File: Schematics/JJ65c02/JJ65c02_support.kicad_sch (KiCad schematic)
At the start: 38 parts, among them J1 Mini-DIN-6, J2 Barrel_Jack, J3 VIA2 PortB, J4 Arduino Jack1, J5 Arduino Jack2, J6 AudioJack2, SW1 RESET, SW2 SW_SPST, U2 NE555, U3 74HC00, U4 MAX232B, U5 74AC138, U6 LM386, U7 LM2940T-5.0/LF08, X1 1Mhz, X2 1.8Mhz

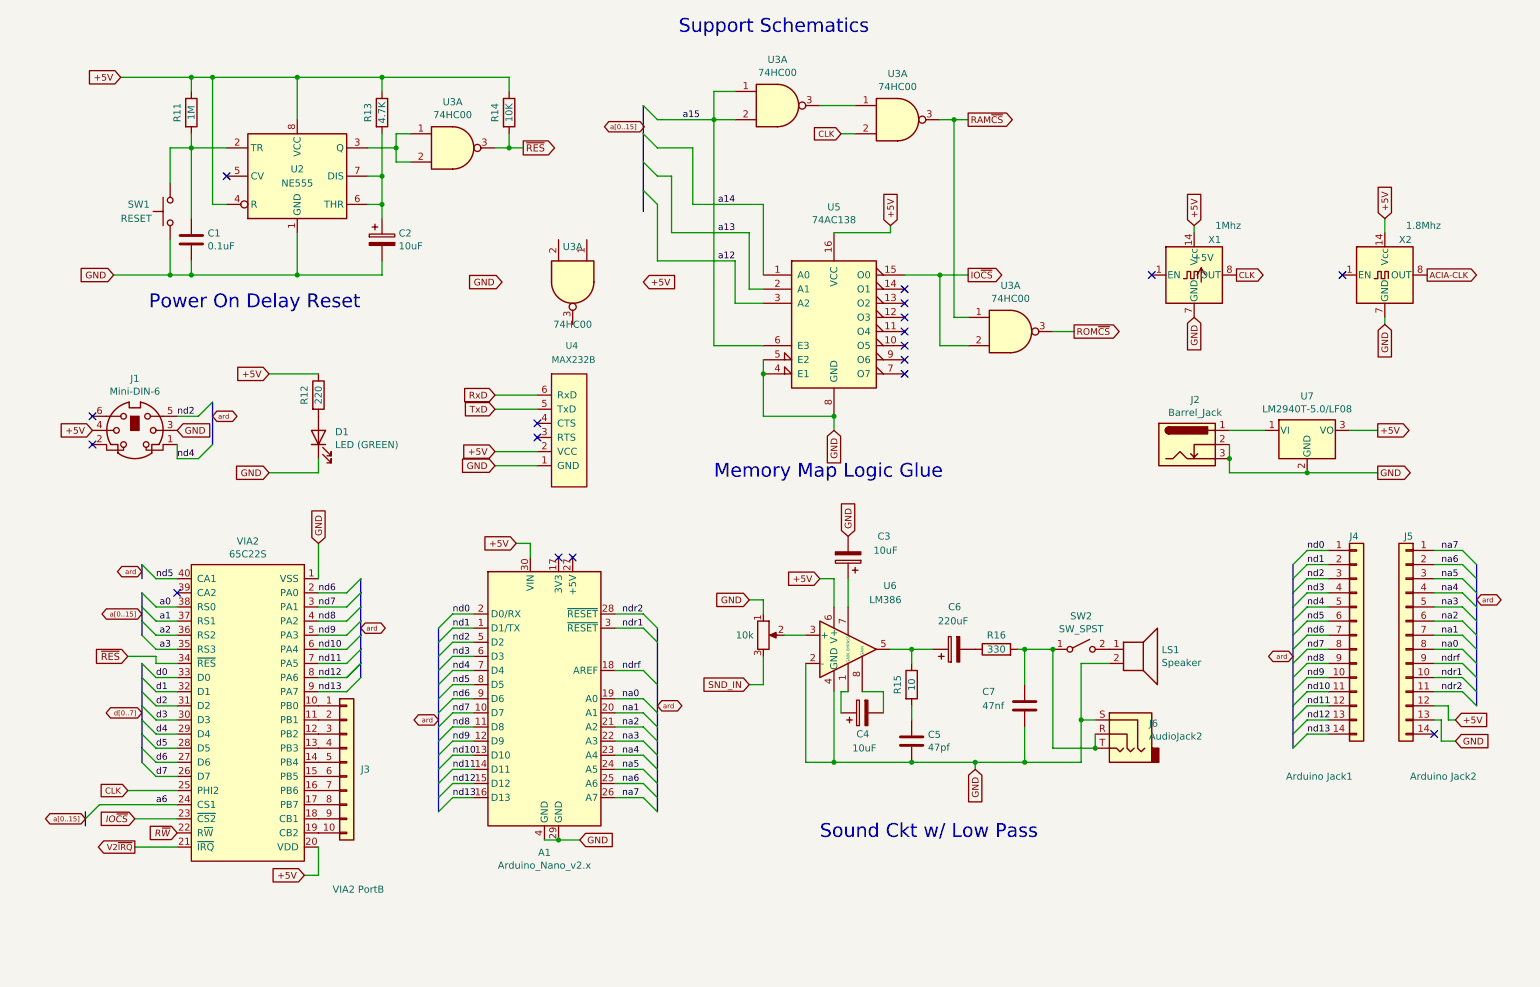
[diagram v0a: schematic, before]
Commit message: We are no longer bit-bashing sound on the VIA chip. Keep the files for future generations
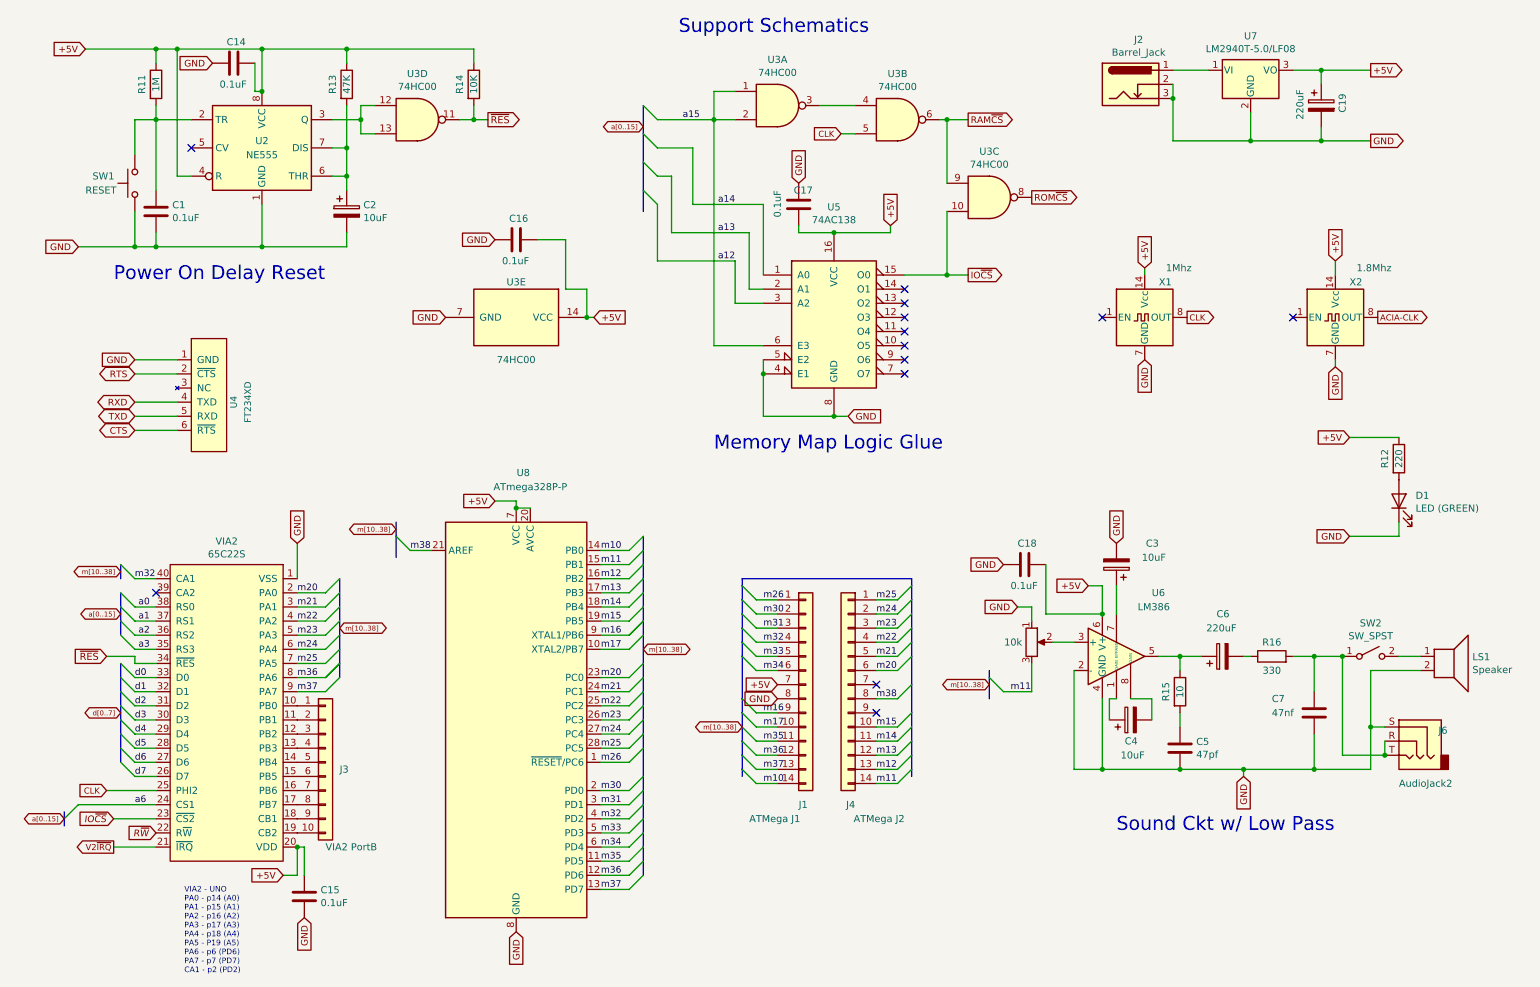
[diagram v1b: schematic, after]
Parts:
- removed A1: Arduino_Nano_v2.x, Module:Arduino_Nano, symbol MCU_Module:Arduino_Nano_v2.x
- removed J1: Mini-DIN-6, JJ65c02:mini_din-6, symbol Connector:Mini-DIN-6
- removed J5: Arduino Jack2, Connector_PinSocket_2.54mm:PinSocket_1x14_P2.54mm_Vertical, symbol Connector_Generic:Conn_01x14
- removed U4: MAX232B, JJ65c02:maxboard, symbol JJ65c02-rescue:MAX232B-6502
- added C14, C15, C16, C17, C18: 0.1uF, Capacitor_THT:C_Disc_D4.7mm_W2.5mm_P5.00mm, symbol Device:C
- added C19: 220uF, Capacitor_THT:CP_Radial_D6.3mm_P2.50mm, symbol Device:C_Polarized
- added J1: ATMega J1, Connector_PinHeader_2.54mm:PinHeader_1x14_P2.54mm_Vertical, symbol Connector_Generic:Conn_01x14
- added U4: FT234XD, JJ65c02:maxboard, symbol JJ65c02-rescue:FT234XD
- added U8: ATmega328P-P, Package_DIP:DIP-28_W7.62mm_Socket, symbol MCU_Microchip_ATmega:ATmega328P-P
- C1, C5, C7: footprint Capacitor_THT:C_Disc_D3.4mm_W2.1mm_P2.50mm -> Capacitor_THT:C_Disc_D4.7mm_W2.5mm_P5.00mm
- C2, C3, C4, C6: symbol Device:CP -> Device:C_Polarized
- J2: footprint Connector_BarrelJack:CUI_PJ-059AH -> Connector_BarrelJack:BarrelJack_Horizontal
- J3: footprint Connector_PinSocket_2.54mm:PinSocket_1x10_P2.54mm_Vertical -> Connector_PinHeader_2.54mm:PinHeader_1x10_P2.54mm_Vertical
- J4: value Arduino Jack1 -> ATMega J2; footprint Connector_PinSocket_2.54mm:PinSocket_1x14_P2.54mm_Vertical -> Connector_PinHeader_2.54mm:PinHeader_1x14_P2.54mm_Vertical
- R13: value 4.7K -> 47K
- RV2: symbol Device:R_POT -> Device:R_Potentiometer
- U7: footprint Connector:LM2940 -> Package_TO_SOT_THT:TO-220-3_Vertical; symbol Regulator_Linear:LM2936-5.0 -> JJ65c02-rescue:LM2940
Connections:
- net +5V: now also U3.14 (VCC), C14.1, C15.1, C16.1, C17.1, C18.1, C19.1, J1.7 (Pin_7), U8.20 (AVCC), U8.7 (VCC)
- net CLK: now also U3.5; no longer U3.2
- net GND: now also U3.7 (GND), C14.2, C15.2, C16.2, C17.2, C18.2, C19.2, J1.8 (Pin_8), U4.1 (GND), U8.22 (GND), U8.8 (GND)
- net IO~{CS}: now also U3.10; no longer U3.2
- net RAM~{CS}: now also U3.6, U3.9; no longer U3.1, U3.3
- net ROM~{CS}: now also U3.8; no longer U3.3
- net ~{RES}: now also U3.11; no longer U3.3
- net at U3.3: now also U3.4; no longer U3.1
- net SND_IN renamed m11
- net m11: now also J4.14 (Pin_14), U8.15 (PB1)
- net nd0 renamed m25
- net m25: now also VIA2.7 (PA5), U8.28 (PC5)
- net nd1 renamed m24
- net m24: now also VIA2.6 (PA4), U8.27 (PC4)
- net nd10 renamed m14
- net m14: now also U8.18 (PB4); no longer VIA2.6 (PA4)
- net nd11 renamed m13
- net m13: now also U8.17 (PB3); no longer VIA2.7 (PA5)
- net nd12 renamed m12
- net m12: now also U8.16 (PB2); no longer VIA2.8 (PA6)
- net nd13 renamed m37
- net m37: now also J1.13 (Pin_13), U8.13 (PD7); no longer J4.14 (Pin_14)
- net nd2 renamed m23
- net m23: now also VIA2.5 (PA3), U8.26 (PC3)
- net nd3 renamed m22
- net m22: now also VIA2.4 (PA2), U8.25 (PC2)
- net nd4 renamed m21
- net m21: now also VIA2.3 (PA1), U8.24 (PC1)
- net nd5 renamed m20
- net m20: now also VIA2.2 (PA0), U8.23 (PC0); no longer VIA2.40 (CA1)
- net nd6: no longer names the net of J4.7 (Pin_7)
- net nd6: no longer VIA2.2 (PA0)
- net nd7 renamed m38
- net m38: now also U8.21 (AREF); no longer VIA2.3 (PA1)
- net nd8: no longer names the net of J4.9 (Pin_9)
- net nd8: no longer VIA2.4 (PA2)
- net nd9 renamed m15
- net m15: now also U8.19 (PB5); no longer VIA2.5 (PA3)
- new net: U2.3 (Q), U3.12, U3.13
- new net CTS: U4.6 (~{RTS})
- new net RTS: U4.2 (~{CTS})
- new net RXD: U4.4 (TXD)
- new net TXD: U4.5 (RXD)
- new net m10: J1.14 (Pin_14), U8.14 (PB0)
- new net m16: J1.9 (Pin_9), U8.9 (XTAL1/PB6)
- new net m17: J1.10 (Pin_10), U8.10 (XTAL2/PB7)
- new net m26: J1.1 (Pin_1), U8.1 (~{RESET}/PC6)
- new net m30: J1.2 (Pin_2), U8.2 (PD0)
- new net m31: J1.3 (Pin_3), U8.3 (PD1)
- new net m32: J1.4 (Pin_4), U8.4 (PD2), VIA2.40 (CA1)
- new net m33: J1.5 (Pin_5), U8.5 (PD3)
- new net m34: J1.6 (Pin_6), U8.6 (PD4)
- new net m35: J1.11 (Pin_11), U8.11 (PD5)
- new net m36: J1.12 (Pin_12), U8.12 (PD6), VIA2.8 (PA6)
- no-connect marks 18 -> 13
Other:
- note added: "VIA2 - UNO PA0 - p14 (A0) PA1 - p15 (A1) PA2 - p16 (A2) PA3 - p17 (A3) PA4 - p18 (A4) PA5 - P19 (A5) PA6 - p6 (PD6) PA7 - p7 (PD7) CA1 - p2 (PD2)"
- moved on the sheet: C1, C2, C3, C4, C5, C6, C7, D1, J2, J3, J6, LS1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

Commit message: Version 3 updates
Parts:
- added C20, C21: 22pf, Capacitor_THT:C_Disc_D4.7mm_W2.5mm_P5.00mm, symbol Device:C
- added Y1: 16Mhz, Crystal:Crystal_HC18-U_Vertical, symbol Device:Crystal
- U7: footprint Package_TO_SOT_THT:TO-220-3_Vertical -> Package_TO_SOT_THT:TO-262-3_Vertical
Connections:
- net +5V: no longer C18.1, U6.6 (V+)
- net GND: now also C20.1, C21.2
- net ~{RES}: now also U8.1 (~{RESET}/PC6)
- net +9V: now reaches J2.1, U7.1 (VI)
- net +9V: now also C18.1, U6.6 (V+)
- net m16: no longer names the net of U8.9 (XTAL1/PB6)
- net m16: now also C20.2, Y1.2; no longer J1.9 (Pin_9)
- net m17: no longer names the net of U8.10 (XTAL2/PB7)
- net m17: now also C21.1, Y1.1; no longer J1.10 (Pin_10)
- net m26: no longer names the net of J1.1 (Pin_1)
- net m26: no longer U8.1 (~{RESET}/PC6)
- no-connect marks 13 -> 16
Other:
- moved on the sheet: C18, C19, C3, C4, C5, C6, C7, D1, J1, J2, J4, J6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

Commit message: Prep for latest round of work:   o Use WinCUPL and ATF22V10C for address decoding   o More RAM and less ROM - new memory map!   o No onboard speaker... wastes space on board
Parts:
- removed LS1: Speaker, JJ65c02:MiniSpeaker, symbol Device:Speaker
- removed SW2: SW_SPST, Button_Switch_THT:SW_DIP_SPSTx01_Slide_6.7x4.1mm_W7.62mm_P2.54mm_LowProfile, symbol Switch:SW_SPST
